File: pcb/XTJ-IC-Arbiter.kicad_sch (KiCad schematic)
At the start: 60 parts, among them IC1 TLV3704IN, J3 DTM13-12PA-R008, U1 LM2675N-5.0/NOPB, U2 CDP68HC68S1, U3 EEC-325X4A, U4 MCP2562-H-P, U5 SP723APP, U6 MCP1700-3302E/TO, U7 DS18B20

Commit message: fix rule violations
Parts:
- R7: value 10kOhm -> 820kOhm
- R8: value 50kOhm -> 4M3ohm
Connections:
- net GND: now also R12.1
- net comp_ref: no longer names the net of XA1.2 (26)
- net speedo_thresh: no longer names the net of XA1.1 (25)
- no-connect marks 7 -> 9
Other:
- note added: "Sensors"
- note removed: "Battery Measure"
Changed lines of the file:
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@@
 		)
 	)
-	(text "Battery Measure"
+	(text "Sensors"
 		(exclude_from_sim no)
 		(at 212.09 72.39 0)
@@
 	)
 	(junction
-		(at 236.22 46.99)
-		(diameter 0)
-		(color 0 0 0 0)
-	)
-	(junction
 		(at 132.08 156.21)
 		(diameter 0)
@@
 	)
 	(junction
-		(at 243.84 29.21)
-		(diameter 0)
-		(color 0 0 0 0)
-	)
-	(junction
 		(at 140.97 147.32)
 		(diameter 0)
@@
 	)
 	(junction
-		(at 199.39 60.96)
-		(diameter 0)
-		(color 0 0 0 0)
-	)
-	(junction
 		(at 179.07 110.49)
 		(diameter 0)
@@
 	)
 	(junction
+		(at 199.39 60.96)
+		(diameter 0)
+		(color 0 0 0 0)
+	)
+	(junction
 		(at 101.6 156.21)
 		(diameter 0)
@@
 	)
 	(no_connect
+		(at 110.49 85.09)
+	)
+	(no_connect
 		(at 88.9 142.24)
 	)
@@
 	)
 	(no_connect
+		(at 110.49 82.55)
+	)
+	(no_connect
 		(at 110.49 97.79)
 	)
@@
 	(wire
 		(pts
-			(xy 254 29.21) (xy 254 41.91)
-		)
-		(stroke
-			(width 0)
-			(type default)
-		)
-	)
-	(wire
-		(pts
 			(xy 243.84 29.21) (xy 210.82 29.21)
 		)
@@
 	(wire
 		(pts
-			(xy 189.23 60.96) (xy 199.39 60.96)
-		)
-		(stroke
-			(width 0)
-			(type default)
-		)
-	)
-	(wire
-		(pts
 			(xy 205.74 33.02) (xy 205.74 39.37)
 		)
@@
 	(wire
 		(pts
-			(xy 204.47 29.21) (xy 204.47 44.45)
+			(xy 195.58 60.96) (xy 199.39 60.96)
 		)
 		(stroke
@@
 	(wire
 		(pts
-			(xy 152.4 93.98) (xy 161.29 93.98)
+			(xy 204.47 29.21) (xy 204.47 44.45)
 		)
 		(stroke
@@
 	(wire
 		(pts
-			(xy 257.81 31.75) (xy 255.27 31.75)
+			(xy 152.4 93.98) (xy 161.29 93.98)
 		)
 		(stroke
@@
 	(wire
 		(pts
-			(xy 189.23 26.67) (xy 195.58 26.67)
+			(xy 257.81 31.75) (xy 255.27 31.75)
 		)
 		(stroke
@@
 	(wire
 		(pts
-			(xy 102.87 49.53) (xy 105.41 49.53)
+			(xy 189.23 26.67) (xy 195.58 26.67)
 		)
 		(stroke
@@
 	(wire
 		(pts
-			(xy 172.72 46.99) (xy 172.72 44.45)
+			(xy 102.87 49.53) (xy 105.41 49.53)
 		)
 		(stroke
@@
 	(wire
 		(pts
-			(xy 146.05 57.15) (xy 146.05 64.77)
+			(xy 172.72 46.99) (xy 172.72 44.45)
 		)
 		(stroke
@@
 	(wire
 		(pts
-			(xy 133.35 64.77) (xy 142.24 64.77)
+			(xy 146.05 57.15) (xy 146.05 64.77)
 		)
 		(stroke
@@
 	(wire
 		(pts
-			(xy 254 29.21) (xy 243.84 29.21)
+			(xy 133.35 64.77) (xy 142.24 64.77)
 		)
 		(stroke
@@
 		)
 	)
-	(wire
+	(polyline
 		(pts
-			(xy 236.22 46.99) (xy 231.14 46.99)
+			(xy 62.23 123.825) (xy 171.45 123.825)
 		)
 		(stroke
@@
 		)
 	)
-	(polyline
+	(wire
 		(pts
-			(xy 62.23 123.825) (xy 171.45 123.825)
+			(xy 195.58 34.29) (xy 195.58 60.96)
 		)
 		(stroke
@@
 		)
 	)
-	(global_label "comp_ref"
-		(shape input)
-		(at 110.49 85.09 180)
-		(fields_autoplaced yes)
-		(effects
-			(font
-				(size 1.27 1.27)
-			)
-			(justify right)
-		)
-		(property "Intersheetrefs" "${INTERSHEET_REFS}"
-			(at 98.8568 85.09 0)
-			(effects
-				(font
-					(size 1.27 1.27)
-				)
-				(justify right)
-				(hide yes)
-			)
-		)
-	)
 	(global_label "can-"
 		(shape input)
@@
 		)
 	)
-	(global_label "speedo_thresh"
-		(shape input)
-		(at 110.49 82.55 180)
-		(fields_autoplaced yes)
-		(effects
-			(font
-				(size 1.27 1.27)
-			)
-			(justify right)
-		)
-		(property "Intersheetrefs" "${INTERSHEET_REFS}"
-			(at 93.9583 82.55 0)
-			(effects
-				(font
-					(size 1.27 1.27)
-				)
-				(justify right)
-				(hide yes)
-			)
-		)
-	)
 	(global_label "IO{slash}1"
 		(shape input)
@@
 			)
 		)
-		(property "Value" "50kOhm"
+		(property "Value" "4M3ohm"
 			(at 238.3278 79.502 90)
 			(effects
@@
 					(size 1.27 1.27)
 				)
-				(justify right)
+				(justify left)
 			)
 		)
@@
 			)
 		)
-		(property "Value" "10kOhm"
+		(property "Value" "820kOhm"
 			(at 248.412 88.392 90)
 			(effects

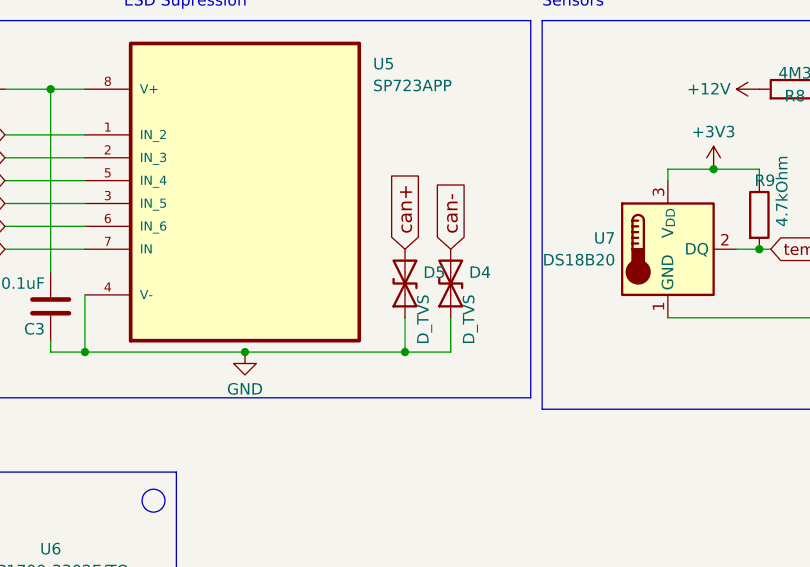
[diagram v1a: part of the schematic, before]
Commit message: Double check and tune board edges
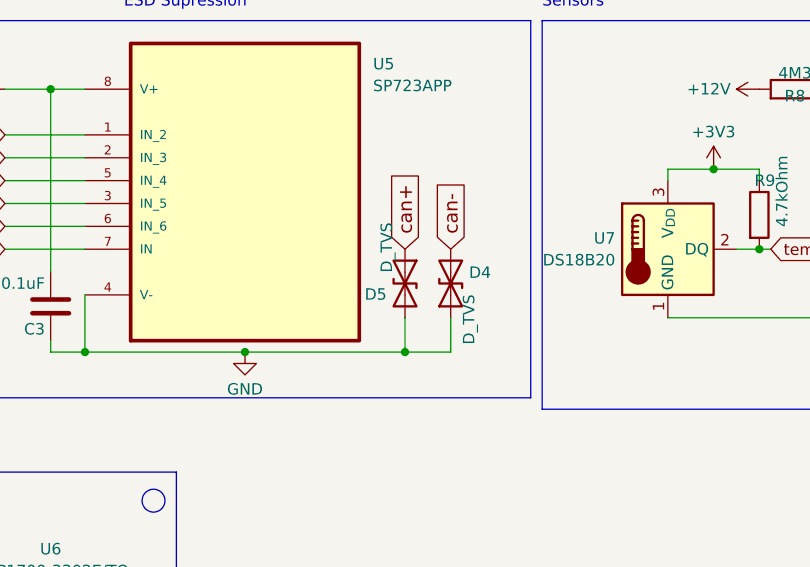
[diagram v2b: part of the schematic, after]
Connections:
- net GND: now also D5.2 (A2); no longer D5.1 (A1)
- net can+: now also D5.1 (A1); no longer D5.2 (A2)
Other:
- moved on the sheet: D5
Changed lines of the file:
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@@
 	(symbol
 		(lib_id "Device:D_TVS")
-		(at 196.85 102.87 90)
+		(at 196.85 102.87 270)
 		(unit 1)
 		(exclude_from_sim no)
@@
 		(dnp no)
 		(property "Reference" "D5"
-			(at 198.882 101.6578 90)
+			(at 194.818 104.0822 90)
 			(effects
 				(font
@@
 		)
 		(property "Value" "D_TVS"
-			(at 198.882 104.0821 0)
+			(at 194.818 101.6579 0)
 			(effects
 				(font

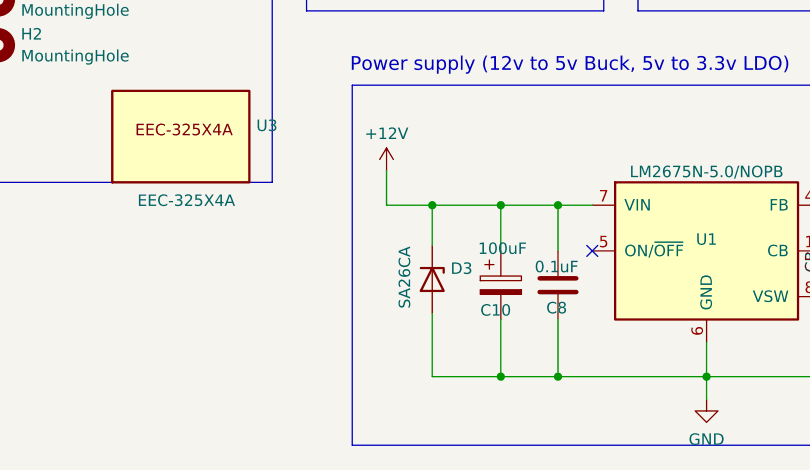
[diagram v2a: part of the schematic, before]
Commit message: Wrong TVS diode for 12v, need only be uni-dir
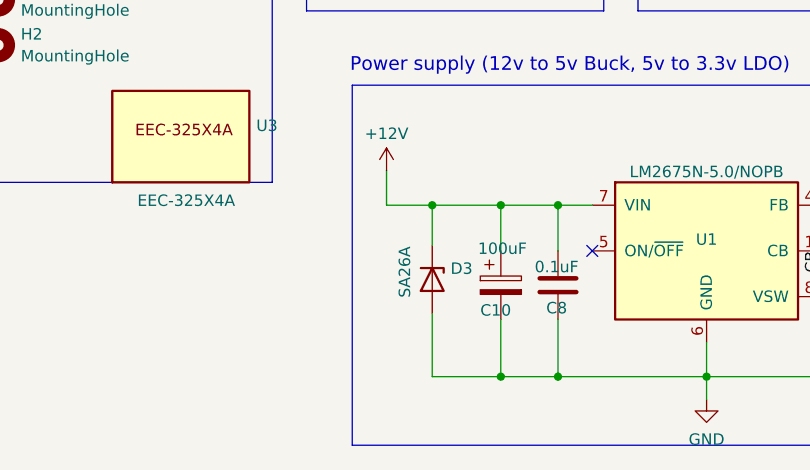
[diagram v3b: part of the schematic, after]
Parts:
- D3: value SA26CA -> SA26A
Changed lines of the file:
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@@
 			)
 		)
-		(property "Value" "SA26CA"
+		(property "Value" "SA26A"
 			(at 68.072 141.732 0)
 			(effects

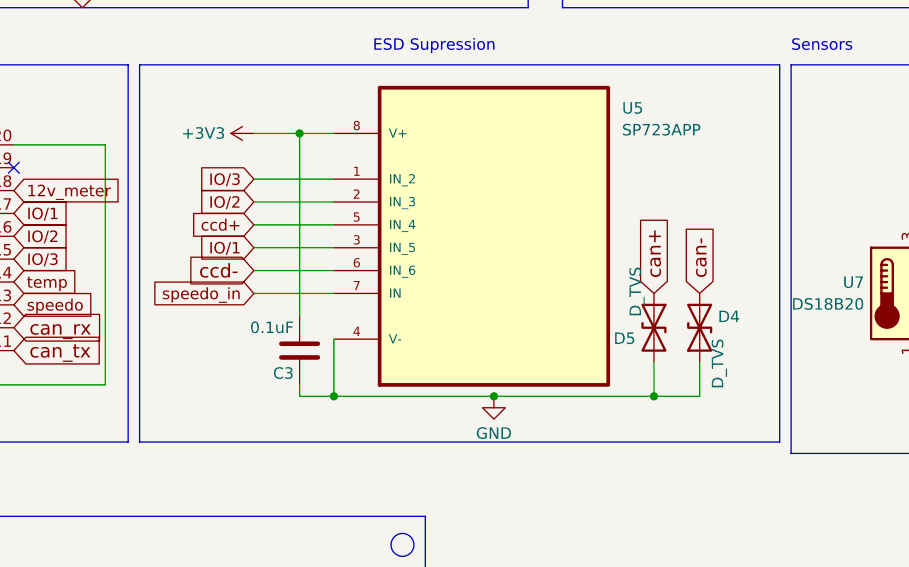
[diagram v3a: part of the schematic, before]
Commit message: delete CAN TVS, as the transceiver has protection equal to the diode array used for other signals
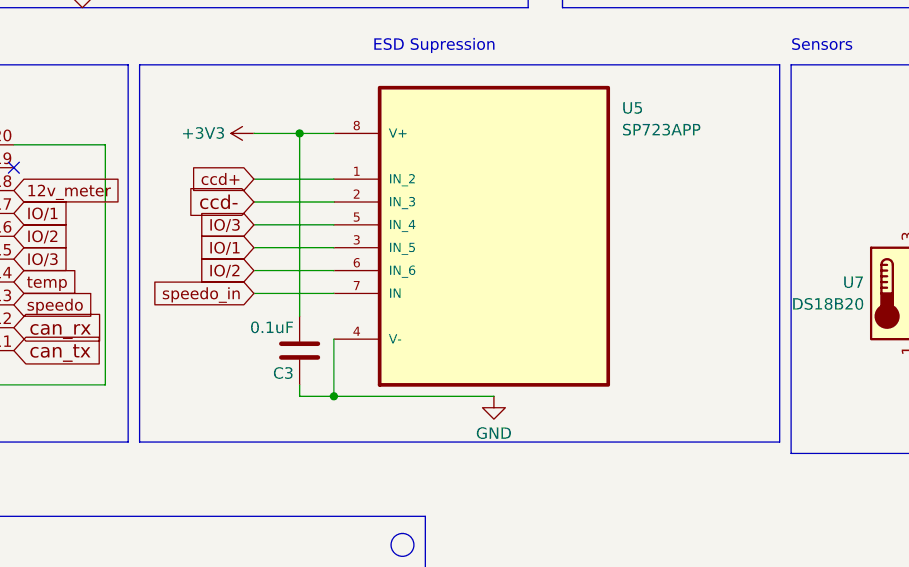
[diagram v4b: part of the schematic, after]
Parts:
- removed D4, D5: D_TVS, Diode_THT:D_DO-41_SOD81_P7.62mm_Horizontal, symbol Device:D_TVS
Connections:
- net IO/2: now also U5.6 (IN_6); no longer U5.2 (IN_3)
- net IO/3: now also U5.5 (IN_4); no longer U5.1 (IN_2)
- net ccd+: now also U5.1 (IN_2); no longer U5.5 (IN_4)
- net ccd-: now also U5.2 (IN_3); no longer U5.6 (IN_6)

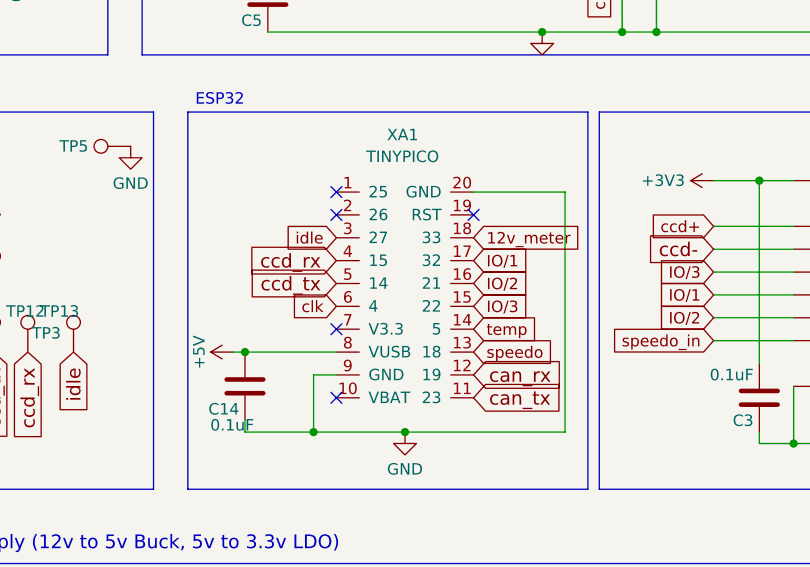
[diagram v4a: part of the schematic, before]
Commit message: reduce ground via tracks
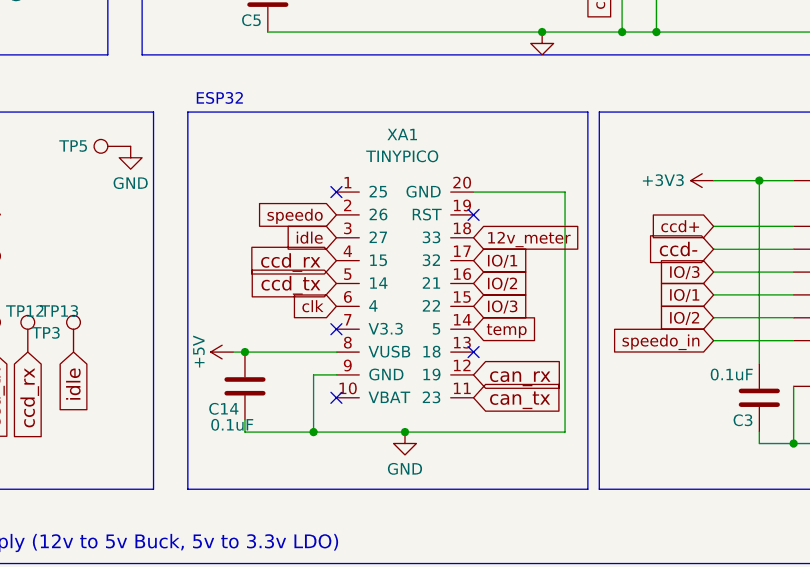
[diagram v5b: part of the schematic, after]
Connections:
- net speedo: now also XA1.2 (26); no longer XA1.13 (18)
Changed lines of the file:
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@@
 	)
 	(no_connect
-		(at 110.49 85.09)
+		(at 125.73 100.33)
 	)
 	(no_connect
@@
 	(global_label "speedo"
 		(shape input)
-		(at 125.73 100.33 0)
+		(at 110.49 85.09 180)
 		(fields_autoplaced yes)
 		(effects
@@
 				(size 1.27 1.27)
 			)
-			(justify left)
-		)
-		(property "Intersheetrefs" "${INTERSHEET_REFS}"
-			(at 135.3675 100.33 0)
-			(effects
-				(font
-					(size 1.27 1.27)
-				)
-				(justify left)
-				(hide yes)
-			)
+			(justify right)
+		)
+		(property "Intersheetrefs" "${INTERSHEET_REFS}"
+			(at 100.8525 85.09 0)
+			(effects
+				(font
+					(size 1.27 1.27)
+				)
+				(justify right)
+				(hide yes)
+			)

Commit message: wip
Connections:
- net can_rx: now also XA1.11 (23); no longer XA1.12 (19)
- net can_tx: now also XA1.12 (19); no longer XA1.11 (23)
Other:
- moved on the sheet: C1, C4, IC1, R10, R12, R6

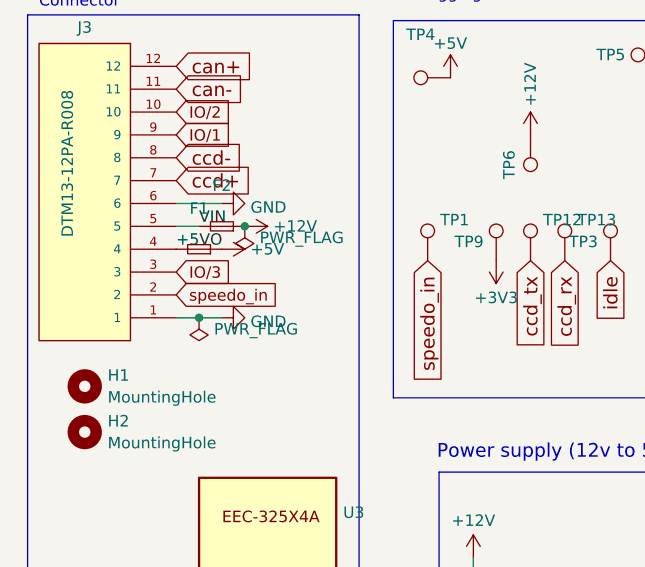
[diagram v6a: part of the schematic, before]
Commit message: Some more routing opt, fix up ref labels
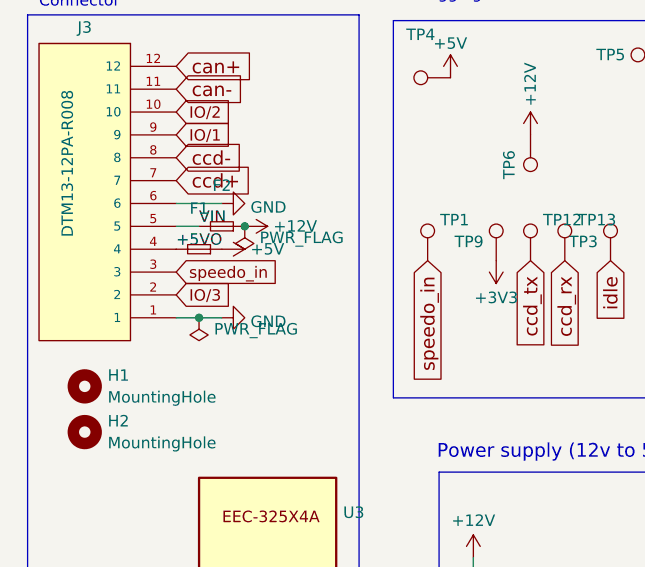
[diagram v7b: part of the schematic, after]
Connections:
- net IO/3: now also J3.2; no longer J3.3
- net speedo_in: now also J3.3; no longer J3.2

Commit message: improve clearance
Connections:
- net IO/1: now also J3.2, XA1.15 (22); no longer J3.9, XA1.17 (32)
- net IO/2: now also J3.3, U5.2 (IN_3); no longer J3.10, U5.6 (IN_6)
- net IO/3: now also J3.10, U5.1 (IN_2), XA1.17 (32); no longer J3.2, U5.5 (IN_4), XA1.15 (22)
- net ccd+: now also U5.7 (IN); no longer U5.1 (IN_2)
- net ccd-: now also U5.6 (IN_6); no longer U5.2 (IN_3)
- net speedo_in: now also J3.9, U5.5 (IN_4); no longer J3.3, U5.7 (IN)
